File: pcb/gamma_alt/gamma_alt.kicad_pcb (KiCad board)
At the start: 2 copper layers, 255 x 45 mm, 232 parts, among them J101 DX07S024WJ3R400, Q201 IRLML0040, Q401 MMBTA42, Q402 MMBTA42, Q403 MMBTA42, T201 ATB322524-0110-T000, U101 LP5907MFX-3.3, U102 AMS1117-3.3, U103 FT231XQ, U104 TPS60400DBV, U201 max1847eee+, U202 TL431, U301 REF35250QDBVR, U302 STM32G474MET6, U303 W25Q64JVSSIQ, U402 ADA4817-1ARDZ, Y301 ABM8G-16.000MHZ-4Y-T3

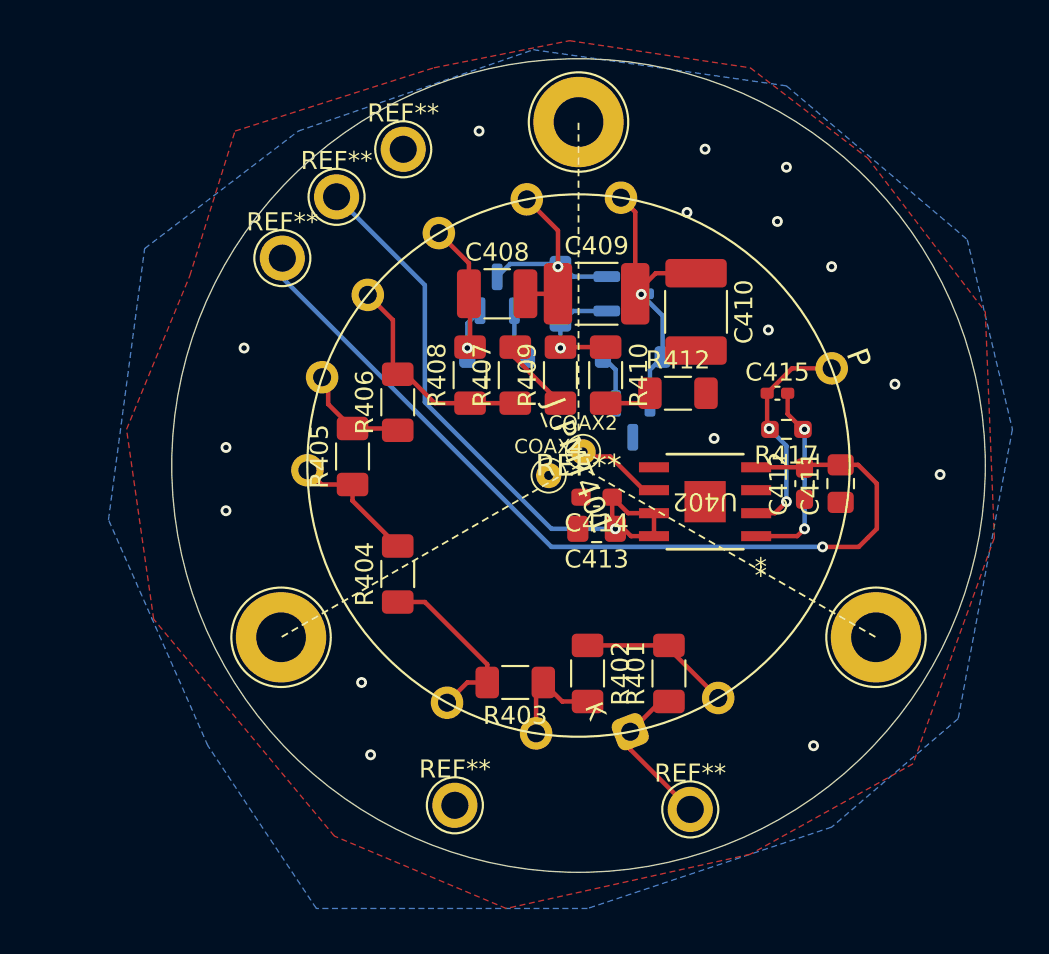
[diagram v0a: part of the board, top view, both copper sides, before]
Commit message: wip(gamma_alt): делитель — итерация v5 (НЕ рабочая, 201 нарушение), план v6 в доке
Итерации: v1=102, v2=43 (лучшая), v3=135, v5=201. Ошибки v5 и план v6 —
в шапке docs/alt_divider_layout.md. Скрипты: scratchpad build/verify_divider.py.
Оригинал pcb/gamma_spectrometer/ не затронут.

Co-Authored-By: Claude Fable 5 <noreply@anthropic.com>
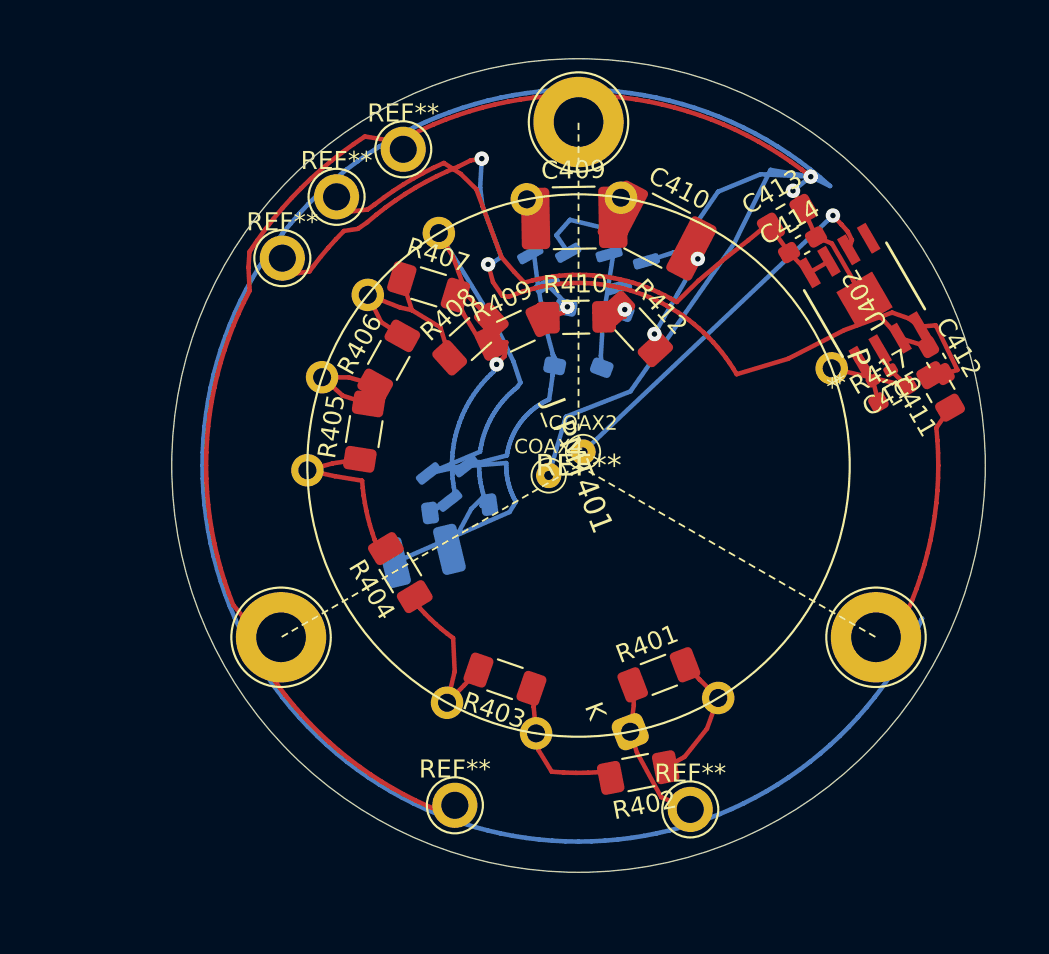
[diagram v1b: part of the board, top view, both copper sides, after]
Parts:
- C408: moved to B.Cu
- moved C413 20.2 mm to (321.5, 86.3), turned to 30 degrees
- moved C414 18.0 mm to (322.4, 87.8), turned to 30 degrees
- moved C408 15.1 mm to (301.3, 105.0), turned to -166.5 degrees
- moved U402 14.2 mm to (325.8, 90.8), turned to 120.1 degrees
- moved Q401 10.4 mm to (303.0, 100.6), turned to 38 degrees
- moved C412 9.98 mm to (329.8, 94.2), turned to -60 degrees
- moved D401 8.65 mm to (303.4, 102.4), turned to 8 degrees
- moved Q403 8.54 mm to (312.9, 89.0), turned to 16 degrees
- moved C411 7.52 mm to (330.0, 95.9), turned to 120 degrees
- moved R407 6.84 mm to (301.7, 90.1), turned to -17 degrees
- moved R417 6.19 mm to (327.4, 96.1), turned to 30 degrees
- moved R402 6.16 mm to (313.3, 117.0), turned to -169 degrees
- moved C415 5.86 mm to (326.8, 95.0), turned to -150 degrees
- moved C410 4.98 mm to (314.3, 87.0), turned to -27.5 degrees
- moved C409 4.38 mm to (309.8, 86.3), turned to 1 degrees
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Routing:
- net GND: track 16.9 -> 272.7 mm, vias 98 -> 86
- net /Divider_Board/DY6: track 9.87 -> 32.1 mm, vias 1 -> 0
- net /Divider_Board/DY7: track 14.4 -> 35.2 mm, vias 1 -> 0
- net AMP_OUT: track 8.30 -> 24.8 mm, vias 0 -> 1
- net Net-(D401-K): track 6.99 -> 16.9 mm, vias 0 -> 1
- net FeedBack: track 10.7 -> 2.52 mm, vias 2 -> 0
- net /Divider_Board/P: track 12.6 -> 6.80 mm, vias 2 -> 0
- net /Divider_Board/DY8: track 16.3 -> 21.4 mm, vias 1 -> 0
- net −5V_A: track 63.7 -> 66.5 mm, vias 1 -> 2
- net /Divider_Board/DY3: track 7.72 -> 10.3 mm
- net /Divider_Board/DY1: track 5.86 -> 8.19 mm
- net Net-(D402-K): track 6.70 -> 5.22 mm
- net /Divider_Board/DY5: track 12.2 -> 11.1 mm
- net /Divider_Board/G: track 8.54 -> 7.59 mm
- net Net-(D403-K): track 5.53 -> 4.75 mm, vias 0 -> 1
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
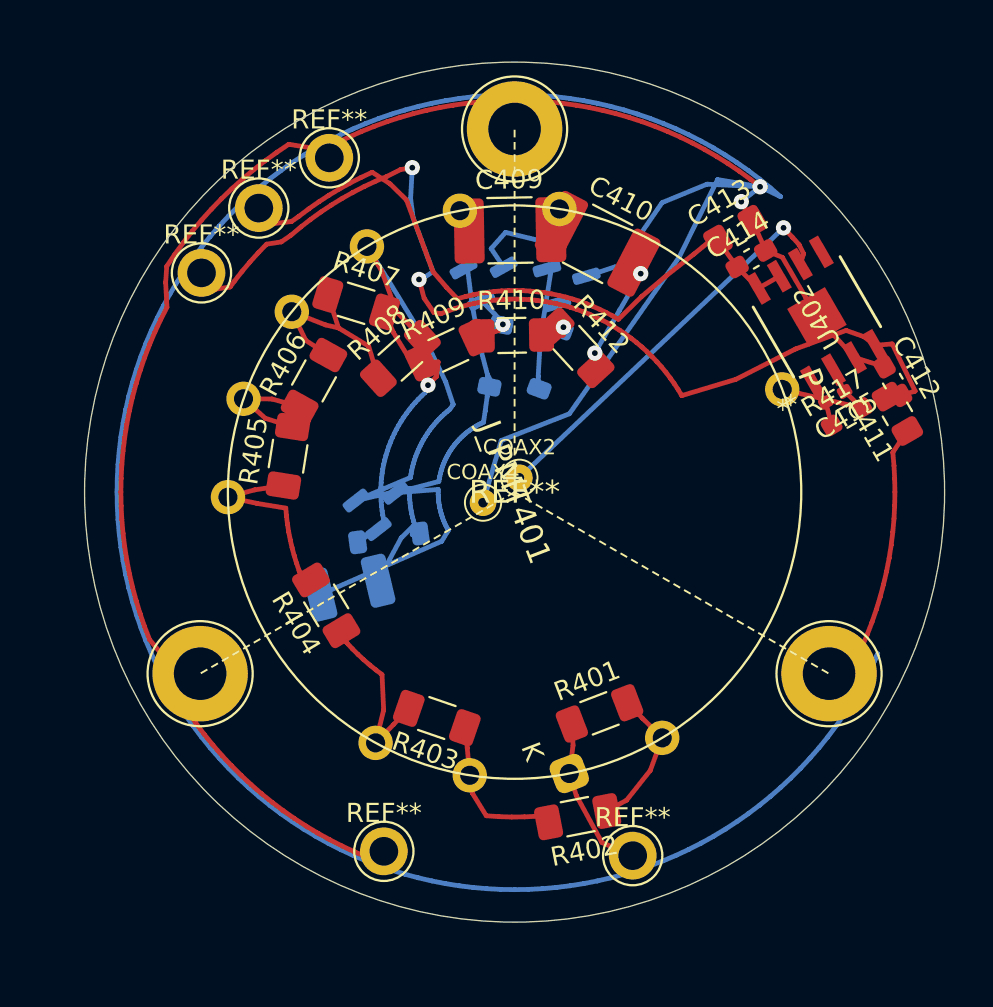
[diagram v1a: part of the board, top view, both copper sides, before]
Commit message: wip(gamma_alt): делитель v12 — питание ±5V решено (горлышко DY6/DY7 + колонна F/B + центральные дуги), 141 локальное нарушение в ячейках
Ключ сессии: доказано, что цанги ±5V заперты в кармане (стойка 270 +
цанга -HV 72 + блок-окружности падов ФЭУ); единственный легальный проход
- щель 0.31 мм между блоками DY6/DY7 @249.9. Обе цепи проведены колонной
(F и B в одном угле) с нулём нарушений. Оригинальная разводка проходит
в 0.6 мм от пада DY5 (680В) - не копировать.

Остаток: утряска B-хвостов ячейки Q401 (пятачок 3x3 мм), C408.2-остров,
мелочь TIA. План следующего захода - в docs/alt_divider_layout.md.

Co-Authored-By: Claude Fable 5 <noreply@anthropic.com>
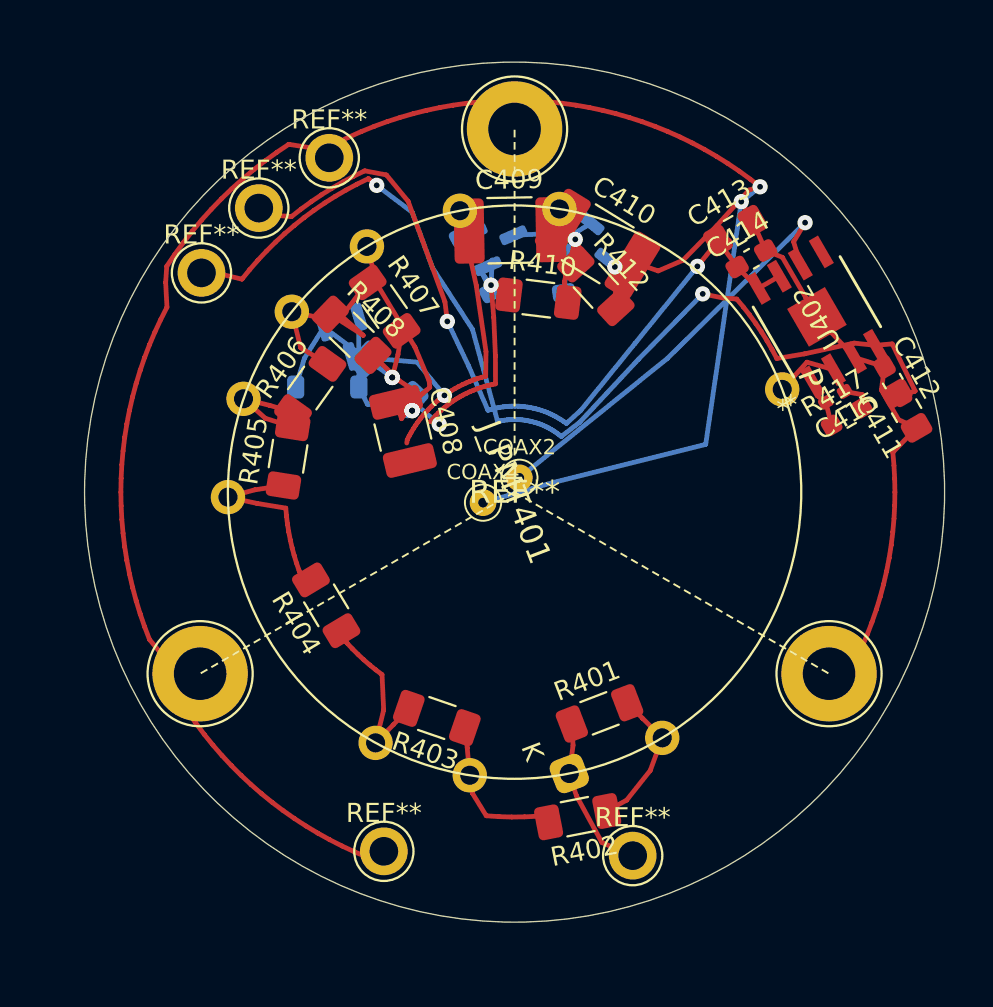
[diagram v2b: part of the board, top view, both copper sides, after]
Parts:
- C408: moved to F.Cu
- R409: moved to B.Cu
- moved Q401 8.80 mm to (301.2, 92.0), turned to -73.5 degrees
- moved C408 8.64 mm to (304.2, 96.8), turned to -76.5 degrees
- moved D401 8.53 mm to (300.2, 94.5), turned to 0 degrees
- moved D403 5.14 mm to (312.3, 87.9), turned to 98 degrees
- moved D402 4.91 mm to (308.0, 88.1), turned to 118.5 degrees
- moved R409 3.49 mm to (303.4, 94.1), turned to -43 degrees
- moved R412 3.41 mm to (314.3, 89.2)
- moved R408 2.83 mm to (301.5, 91.8), turned to -44 degrees
- moved R410 2.37 mm to (311.2, 89.9), turned to -7 degrees
- moved Q403 2.14 mm to (314.1, 87.3), turned to -39 degrees
- moved Q402 1.82 mm to (309.1, 86.9), turned to 23.5 degrees
- moved R407 1.51 mm to (303.2, 90.3), turned to -55 degrees
- moved C411 0.51 mm to (330.5, 95.7)
- moved R406 0.42 mm to (299.3, 94.6), turned to 54.5 degrees
- turned C410 to -31.5 degrees
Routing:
- net GND: track 272.7 -> 162.5 mm, vias 86 -> 85
- net Net-(D402-K): track 5.22 -> 16.4 mm, vias 1 -> 2
- net /Divider_Board/DY8: track 21.4 -> 11.6 mm
- net /Divider_Board/DY6: track 32.1 -> 22.5 mm, vias 0 -> 2
- net /Divider_Board/DY7: track 35.2 -> 26.9 mm, vias 0 -> 1
- net +5V_A: track 68.9 -> 77.0 mm, vias 1 -> 3
- net Net-(D401-K): track 16.9 -> 10.4 mm, vias 1 -> 2
- net Net-(D403-K): track 4.75 -> 9.17 mm
- net −5V_A: track 66.5 -> 68.5 mm
- net AMP_OUT: track 24.8 -> 26.0 mm
- net /Divider_Board/DY5: track 11.1 -> 12.0 mm
- net /Divider_Board/P: track 6.80 -> 6.29 mm
